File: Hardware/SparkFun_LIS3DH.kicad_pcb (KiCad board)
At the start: 2 copper layers, 25.4 x 25.4 mm, 62 parts, among them J1 Conn_01x02, J2 Conn_01x05, J3 Qwiic_RA, J4 I2C, J5 Qwiic_RA, U1 LIS3DH

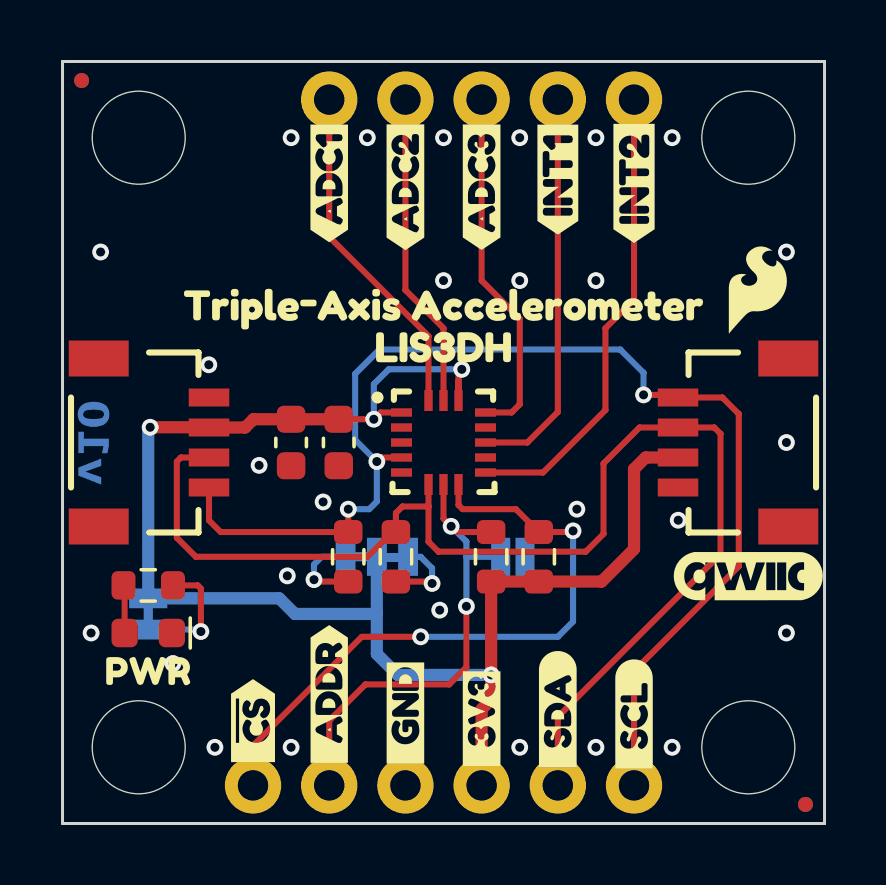
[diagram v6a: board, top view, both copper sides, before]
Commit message: Addes axes to the IU
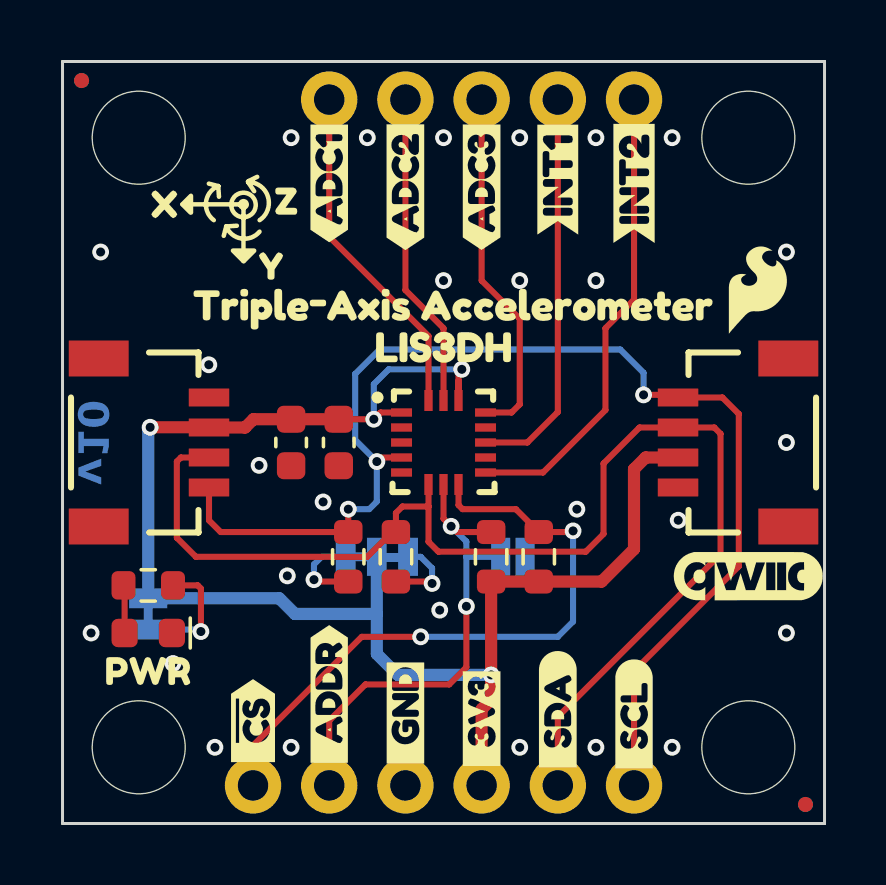
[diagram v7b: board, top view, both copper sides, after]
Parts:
- removed the G*** at (146.1, 102.6)
- removed kibuzzard-684893BE: G***, kibuzzard-684893BE
- removed kibuzzard-684893C6: G***, kibuzzard-684893C6
- removed kibuzzard-684893E9: G***, kibuzzard-684893E9
- removed kibuzzard-684893FA: G***, kibuzzard-684893FA
- added kibuzzard-685C51A0: G***, kibuzzard-685C51A0, F.Cu at (126.7, 90.2)
- added kibuzzard-685C51A0: G***, kibuzzard-685C51A0, B.Cu at (125.5, 91.3)
- added kibuzzard-685C52CC: G***, kibuzzard-685C52CC, F.Cu at (130.2, 92.2)
- added kibuzzard-685C52CC: G***, kibuzzard-685C52CC, B.Cu at (129.0, 93.4)
- added kibuzzard-685C52E1: G***, kibuzzard-685C52E1, F.Cu at (130.7, 90.1)
- added kibuzzard-685C52E1: G***, kibuzzard-685C52E1, B.Cu at (129.6, 91.4)
- added kibuzzard-685C549D: G***, kibuzzard-685C549D, F.Cu at (139.8, 89.3)
- added kibuzzard-685C54A5: G***, kibuzzard-685C54A5, F.Cu at (142.3, 89.5)
- added kibuzzard-685C54B5: G***, kibuzzard-685C54B5, B.Cu at (139.8, 89.3)
- added kibuzzard-685C54BC: G***, kibuzzard-685C54BC, B.Cu at (142.3, 89.5)
- moved kibuzzard-68376F54 0.32 mm to (136.3, 93.7)

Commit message: Moves v10 in board, updates IC symbol, and fixes various text
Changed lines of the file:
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@@
 	)
 	(gr_text "v10"
-		(at 124.264 98.106 -90)
+		(at 147.396 98.106 90)
 		(layer "B.Cu" knockout)
 		(effects
@@
 	)
 	(via
-		(at 147.396 98.106)
-		(size 0.56)
-		(drill 0.3)
+		(at 124.2185 98.106)
+		(size 0.56)
+		(drill 0.3)
